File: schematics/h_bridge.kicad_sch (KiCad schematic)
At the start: 12 parts, among them U3 L298HN

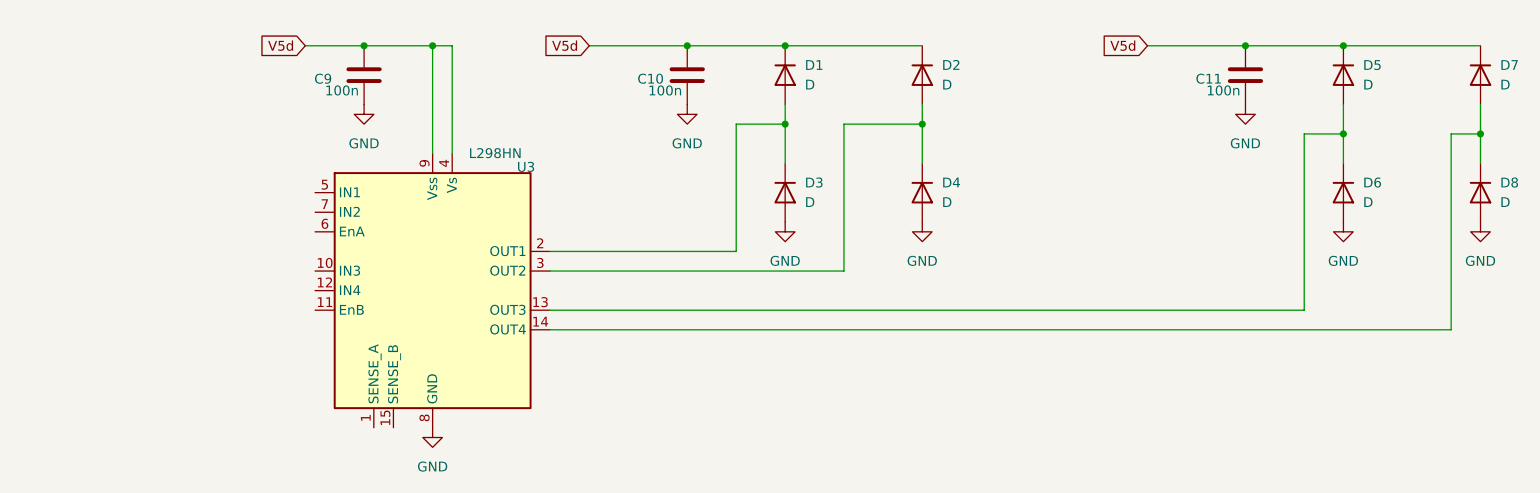
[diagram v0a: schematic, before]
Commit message: changed format to kicad project
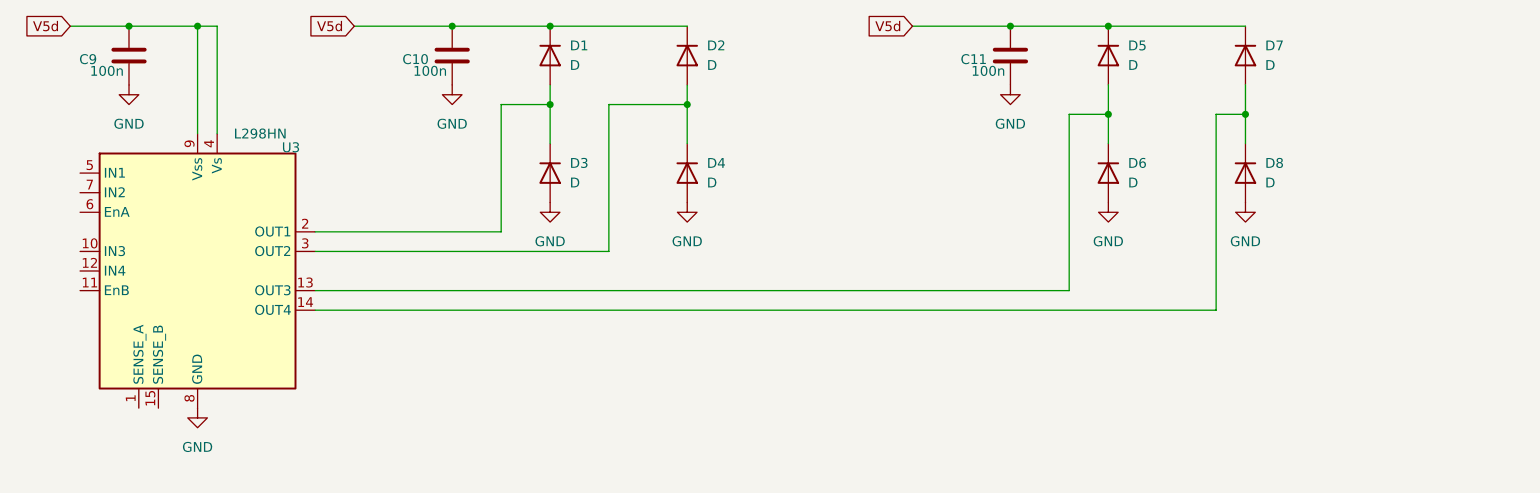
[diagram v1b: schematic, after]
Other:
- moved on the sheet: C10, C11, C9, D1, D2, D3, D4, D5, D6, D7, D8, U3
